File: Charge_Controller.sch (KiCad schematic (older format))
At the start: 147 parts, among them J1 SOLAR, J10 Conn_01x01_Female, J11 Conn_01x01_Female, J12 Conn_01x01_Female, J13 Conn_01x01_Female, J14 Conn_01x01_Female, J15 Conn_01x01_Female, J16 Conn_01x01_Female, J17 Conn_01x01_Female, J18 Conn_01x01_Female, J19 Conn_01x01_Female, J2 Conn_01x01_Female, J20 Conn_01x01_Female, J21 Conn_01x01_Female, J22 Conn_01x01_Female, J23 Conn_01x01_Female, J24 Conn_01x01_Female, J25 Conn_01x01_Female, J26 Conn_01x01_Female, J27 Conn_01x01_Female, J28 Conn_01x01_Female, J29 Conn_01x01_Female, J3 Conn_01x01_Female, J30 Conn_01x01_Female, J31 Conn_01x01_Female, J32 Conn_01x01_Female, J33 SOLAR, J34 BATT, J35 BATT, J36 FAN, J37 I2C_CON, J38 I2C_CON, J4 Conn_01x01_Female, J5 Conn_01x01_Female, J6 Conn_01x01_Female, J7 Conn_01x01_Female, J8 BATT, J9 USB_OTG, Q1 CSD19505, Q2 CSD19505, Q3 CSD19505, Q4 Si2306, Q5 2N3904, Q6 2N3904, Q7 PMOS-100V-78A, Q8 PMOS-100V-78A, Q9 Si2306, SW1 RIGHT, SW2 RIGHT, SW3 RIGHT, SW4 RIGHT, U1 ACS712-30A, U10 ADS1015, U11 NUP4202, U2 B1212, U3 AMS1117-5.0, U4 AMS1117-3.3, U5 XL7005A, U6 XL7005A, U7 IR2104, U8 ESP32-WROOM-32, U9 CH340G

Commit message: Initial draft layout, no traces yet, but parts are mostly arranged.
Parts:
- SW2: value RIGHT -> LEFT
- SW3: value RIGHT -> BACK
- SW4: value RIGHT -> SELECT
- U9: value CH340G -> CH340C; footprint Package_SO:SOIC-16_3.9x9.9mm_P1.27mm -> Package_SO:STC_SOP-16_3.9x9.9mm_P1.27mm; jlcpcb C14267 -> C84681
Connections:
- net +3V3: now also SW4.2
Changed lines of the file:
@@
 P 8625 1600
 F 0 "U9" H 8850 1050 50  0000 C CNN
-F 1 "CH340G" V 8625 1575 50  0000 C CNN
-F 2 "Package_SO:SOIC-16_3.9x9.9mm_P1.27mm" H 8675 1050 50  0001 L CNN
+F 1 "CH340C" V 8625 1575 50  0000 C CNN
+F 2 "Package_SO:STC_SOP-16_3.9x9.9mm_P1.27mm" H 8675 1050 50  0001 L CNN
 F 3 "http://www.datasheet5.com/pdf-local-2195953" H 8275 2400 50  0001 C CNN
-F 4 "C14267" H 8625 1600 50  0001 C CNN "jlcpcb"
+F 4 "C84681" H 8625 1600 50  0001 C CNN "jlcpcb"
 	1    8625 1600
 	1    0    0    -1
@@
 P 5325 7475
 F 0 "SW2" H 5100 7550 50  0000 C CNN
-F 1 "RIGHT" H 5325 7669 50  0001 C CNN
+F 1 "LEFT" H 5325 7669 50  0001 C CNN
 F 2 "Button_Switch_SMD:SW_SPST_EVQQ2" H 5325 7675 50  0001 C CNN
 F 3 "~" H 5325 7675 50  0001 C CNN
@@
 P 5325 7650
 F 0 "SW3" H 5100 7725 50  0000 C CNN
-F 1 "RIGHT" H 5325 7844 50  0001 C CNN
+F 1 "BACK" H 5325 7844 50  0001 C CNN
 F 2 "Button_Switch_SMD:SW_SPST_EVQQ2" H 5325 7850 50  0001 C CNN
 F 3 "~" H 5325 7850 50  0001 C CNN
@@
 P 5325 7825
 F 0 "SW4" H 5100 7900 50  0000 C CNN
-F 1 "RIGHT" H 5325 8019 50  0001 C CNN
+F 1 "SELECT" H 5325 8019 50  0001 C CNN
 F 2 "Button_Switch_SMD:SW_SPST_EVQQ2" H 5325 8025 50  0001 C CNN
 F 3 "~" H 5325 8025 50  0001 C CNN
@@
 $EndComp
 Wire Wire Line
-	5525 7800 5525 7650
-Wire Wire Line
 	5525 7275 5650 7275
 Connection ~ 5525 7275
@@
 Wire Wire Line
 	7150 1500 8225 1500
+Wire Wire Line
+	5525 7650 5525 7825
 $EndSCHEMATC

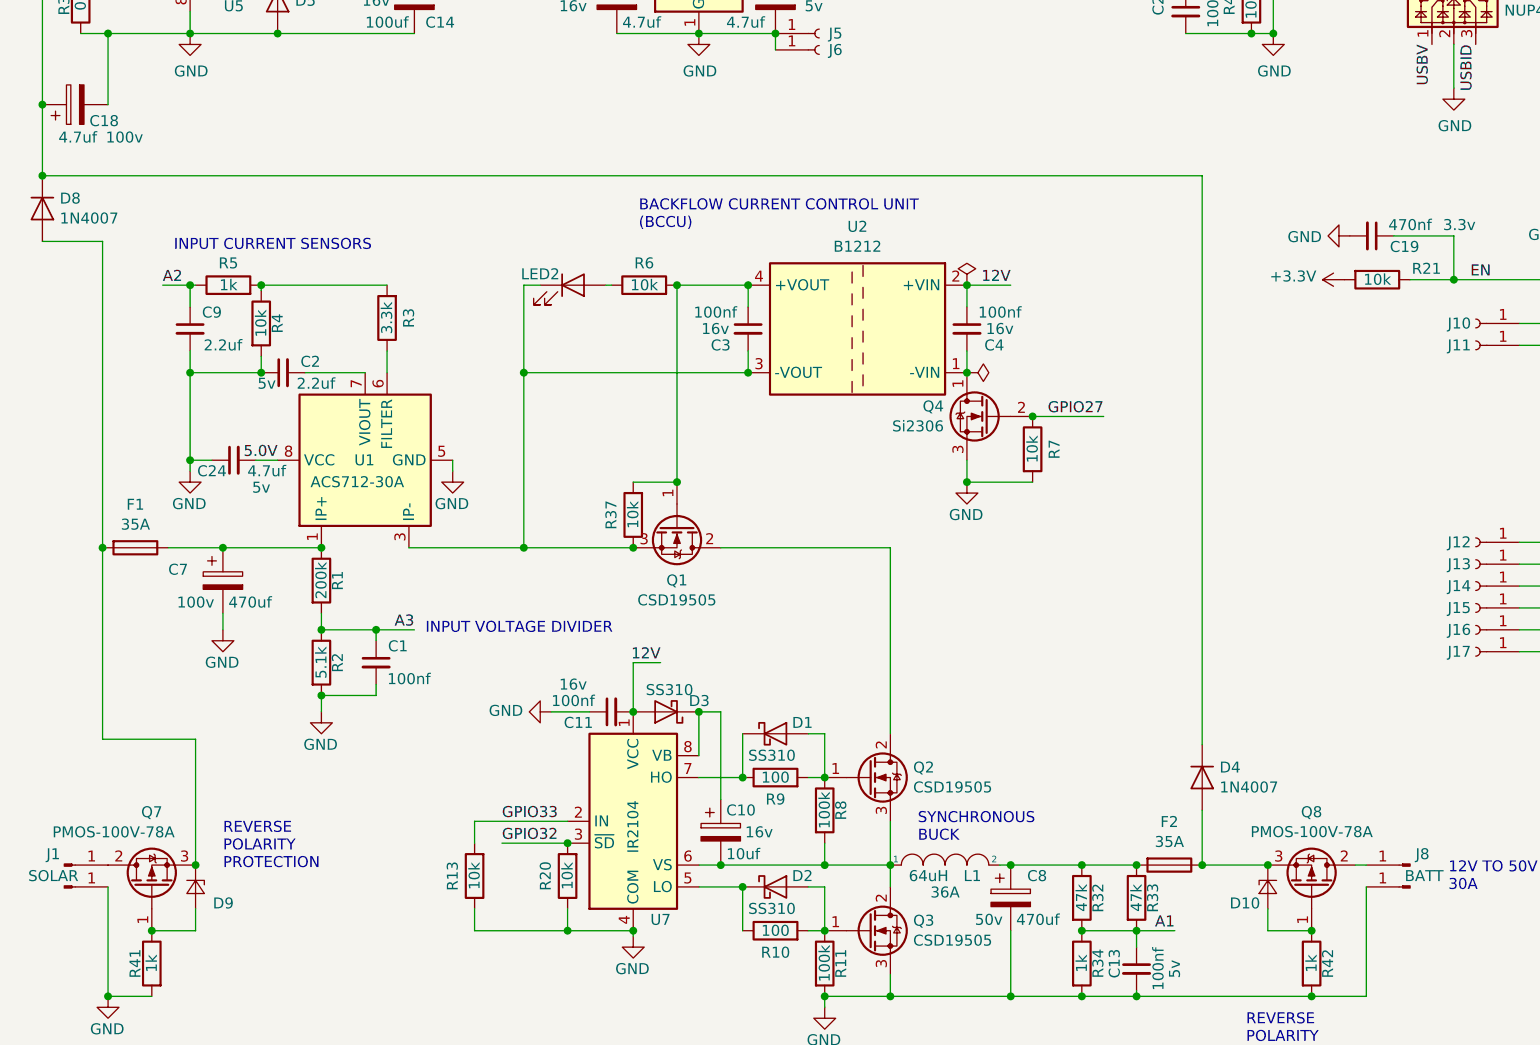
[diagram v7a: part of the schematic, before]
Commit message: More PCB initial setup, 2oz copper, widths, via's etc.
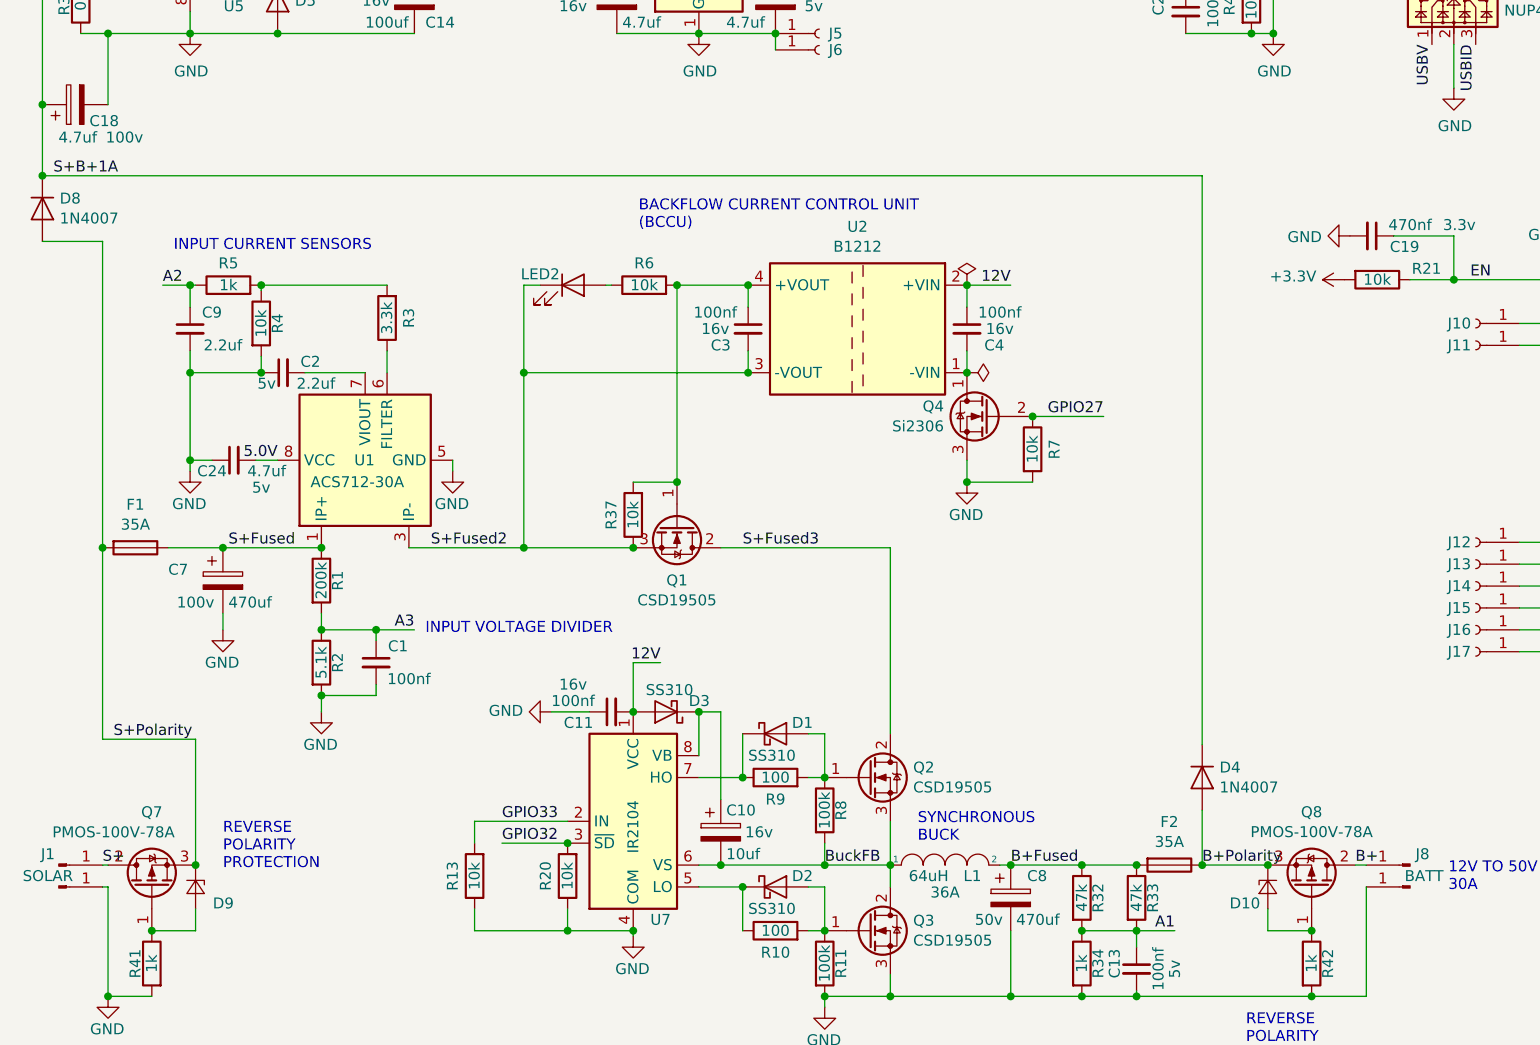
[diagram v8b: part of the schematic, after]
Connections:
- net S+B+1A: now reaches C18.1, D4.1 (K), D8.1 (K), U5.1 (VIN), U6.1 (VIN)
- net S+Fused2: now reaches C3.2, LED2.1 (K), Q1.3 (S), R37.1, U1.3 (IP-), U1.4 (IP-), U2.3 (-VOUT)
- net BuckFB: now reaches C10.2, L1.1, Q2.3 (S), Q3.2 (D), R8.2, U7.6 (VS)
- net B+Fused: now reaches C8.1, F2.2, L1.2, R32.1, R33.1
- net S+Fused: now reaches C7.1, F1.1, R1.1, U1.1 (IP+), U1.2 (IP+)
- net S+Polarity: now reaches D8.2 (A), D9.1 (K), F1.2, Q7.3 (S)
- net S+: now reaches J1.1 (Pin_1), Q7.2 (D)
- net B+: now reaches J8.1 (Pin_1), Q8.2 (D)
- net B+Polarity: now reaches D10.1 (K), D4.2 (A), F2.1, Q8.3 (S)
- net S+Fused3: now reaches Q1.2 (D), Q2.2 (D)
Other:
- moved on the sheet: J1
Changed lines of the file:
@@
 L Connector:Conn_01x01_Male J1
 U 1 1 6328B187
-P 700 6000
-F 0 "J1" H 650 6050 50  0000 C CNN
-F 1 "SOLAR" H 650 5950 50  0000 C CNN
-F 2 "TestPoint:TestPoint_Keystone_5005-5009_Compact" H 700 6000 50  0001 C CNN
-F 3 "~" H 700 6000 50  0001 C CNN
-F 4 "277-13746-ND" H 700 6000 50  0001 C CNN "Digikey"
-F 5 "NA" H 700 6000 50  0001 C CNN "jlcpcb"
-	1    700  6000
+P 675 6000
+F 0 "J1" H 625 6050 50  0000 C CNN
+F 1 "SOLAR" H 625 5950 50  0000 C CNN
+F 2 "TestPoint:TestPoint_Keystone_5005-5009_Compact" H 675 6000 50  0001 C CNN
+F 3 "~" H 675 6000 50  0001 C CNN
+F 4 "277-13746-ND" H 675 6000 50  0001 C CNN "Digikey"
+F 5 "NA" H 675 6000 50  0001 C CNN "jlcpcb"
+	1    675  6000
 	1    0    0    -1
 $EndComp
@@
 L Connector:Conn_01x01_Male J33
 U 1 1 63DCA583
-P 700 6100
-F 0 "J33" H 650 6050 50  0001 C CNN
-F 1 "SOLAR" H 650 6050 50  0001 C CNN
-F 2 "TestPoint:TestPoint_Keystone_5005-5009_Compact" H 700 6100 50  0001 C CNN
-F 3 "~" H 700 6100 50  0001 C CNN
-F 4 "NA" H 700 6100 50  0001 C CNN "Digikey"
-F 5 "NA" H 700 6100 50  0001 C CNN "jlcpcb"
-	1    700  6100
+P 675 6100
+F 0 "J33" H 625 6050 50  0001 C CNN
+F 1 "SOLAR" H 625 6050 50  0001 C CNN
+F 2 "TestPoint:TestPoint_Keystone_5005-5009_Compact" H 675 6100 50  0001 C CNN
+F 3 "~" H 675 6100 50  0001 C CNN
+F 4 "NA" H 675 6100 50  0001 C CNN "Digikey"
+F 5 "NA" H 675 6100 50  0001 C CNN "jlcpcb"
+	1    675  6100
 	1    0    0    -1
 $EndComp
@@
 Wire Wire Line
 	5525 7650 5525 7825
+Wire Wire Line
+	875  6000 900  6000
+Wire Wire Line
+	875  6100 900  6100
+Text Label 875  6000 0    50   ~ 0
+S+
+Text Label 925  5425 0    50   ~ 0
+S+Polarity
+Text Label 1450 4550 0    50   ~ 0
+S+Fused
+Text Label 650  2850 0    50   ~ 0
+S+B+1A
+Text Label 6600 6000 0    50   ~ 0
+B+
+Text Label 5900 6000 0    50   ~ 0
+B+Polarity
+Text Label 5025 6000 0    50   ~ 0
+B+Fused
+Text Label 2375 4550 0    50   ~ 0
+S+Fused2
+Text Label 3800 4550 0    50   ~ 0
+S+Fused3
+Text Label 4175 6000 0    50   ~ 0
+BuckFB
 $EndSCHEMATC
